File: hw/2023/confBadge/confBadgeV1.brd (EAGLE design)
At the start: 96.5 x 78.7 mm, 51 parts, among them J1 10118192-0002LF, Q1 8/16/20MHz, U1 ATMEGA328, U10 WS2812-2020, U11 WS2812-2020, U12 WS2812-2020, U13 WS2812-2020, U14 WS2812-2020, U15 WS2812-2020, U16 WS2812-2020, U17 WS2812-2020, U18 WS2812-2020, U19 WS2812-2020, U2 AP2112-3.3, U20 WS2812-2020, U3 WS2812-2020, U4 WS2812-2020, U5 PCM12SMTRPCM12SMTR_CNK, U6 24792479PCB_37P49X52P63_KEY, U7 CH340C, U8 SMF05CT1G, U9 WS2812-2020

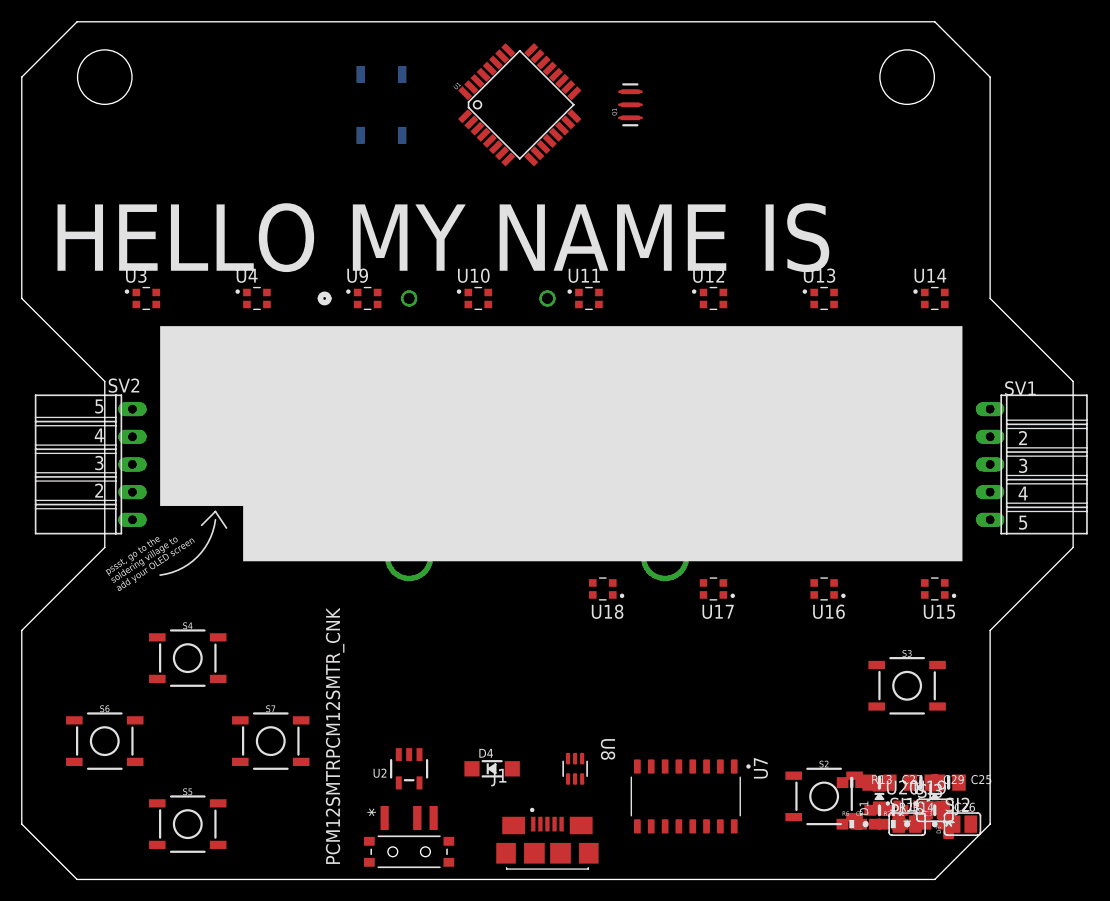
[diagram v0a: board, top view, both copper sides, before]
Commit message: Completed part placement
- parts placement done
-added cap to each neopixel
- connected usb power to regulator
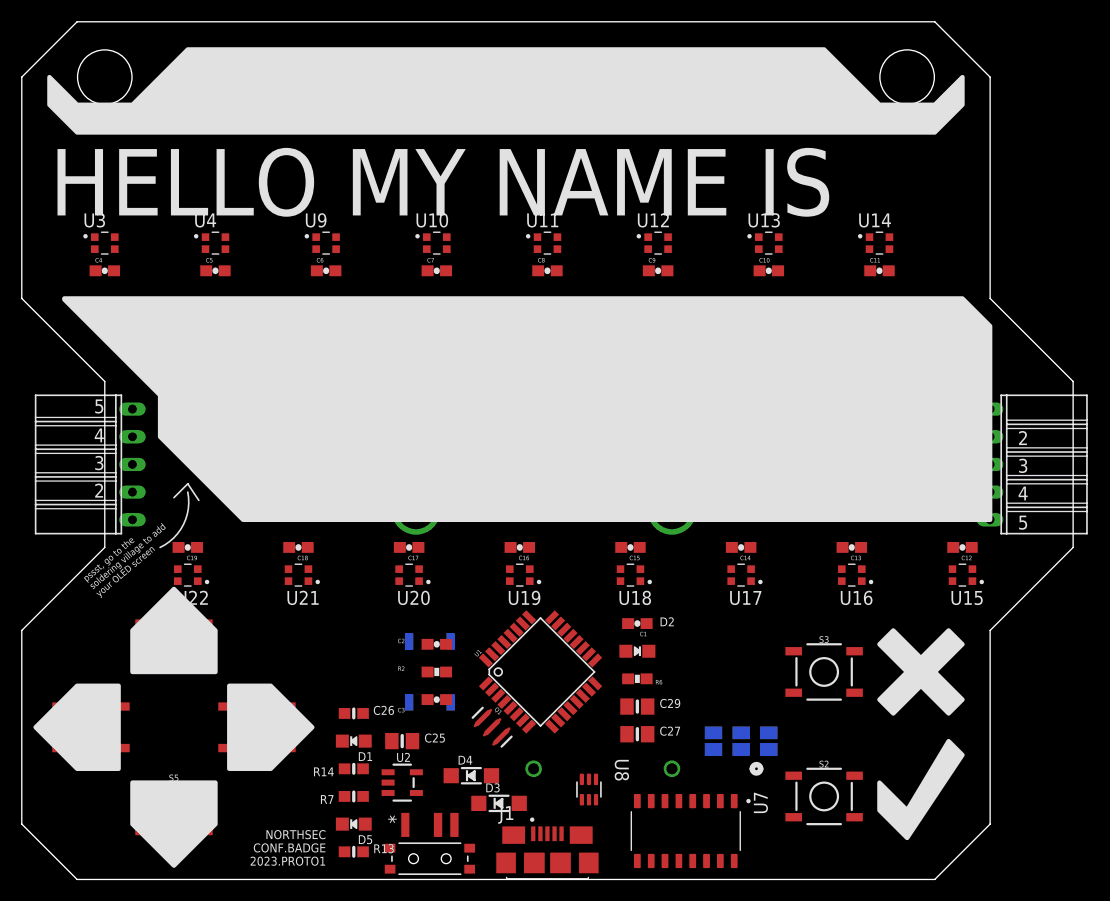
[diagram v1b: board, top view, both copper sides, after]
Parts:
- added C10, C11, C12, C13, C14, C15, C16, C17, C18, C19, C4, C5, C6, C7, C8, C9: 0.1uF, SparkFun:0603-CAP
- added D2: RED, microbuilder:CHIPLED_0805_NOOUTLINE
- added U21, U22: WS2812-2020, WS2812-2020:LED_WS2812-2020
- D3: value Green -> MBR120; device Testing:0603-LED-ALT1 -> microbuilder:SOD-123
- moved Q1 58.5 mm to (43.2, 14.0), turned to 315 degrees
- moved C26 54.1 mm to (30.5, 15.2)
- moved D5 53.4 mm to (30.5, 5.08), turned to 90 degrees
- moved S1 52.3 mm to (37.5, 19.1)
- moved U1 52.1 mm to (47.6, 19.1)
- moved U20 50.6 mm to (35.6, 27.9), turned to 180 degrees
- moved C25 50.3 mm to (34.9, 12.7)
- moved R14 49.7 mm to (30.5, 10.2), turned to 180 degrees
- moved U6 49.5 mm to (59.7, 10.2), turned to 0 degrees
- moved D1 48.5 mm to (30.5, 12.7), turned to 90 degrees
- moved R7 48.3 mm to (30.5, 7.62), turned to 180 degrees
- moved C3 47.1 mm to (38.1, 16.5), turned to 180 degrees
- moved R13 46.2 mm to (30.5, 2.54)
- moved R2 44.2 mm to (38.1, 19.1), turned to 180 degrees
- moved U19 43.8 mm to (45.7, 27.9), turned to 180 degrees
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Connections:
- removed net VCC: C3.2
- new net N$17: U20.1, U21.3
- new net N$20: U21.1, U22.3
- net 3.3V: now also C3.2
- net GND: now also C10.1, C11.1, C12.1, C13.1, C14.1, C15.1, C16.1, C17.1, C18.1, C19.1, C4.1, C5.1, C6.1, C7.1, C8.1, C9.1, D2.C, U21.2, U22.2; no longer D3.C
- net N$34: now also D3.C
- net N$7: now also D2.A; no longer D3.A
- net VBUS: now also D3.A
- net VDD: now also C10.2, C11.2, C12.2, C13.2, C14.2, C15.2, C16.2, C17.2, C18.2, C19.2, C4.2, C5.2, C6.2, C7.2, C8.2, C9.2, U21.4, U22.4
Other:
- board text added: "NORTHSEC CONF.BADGE 2023.PROTO1"
